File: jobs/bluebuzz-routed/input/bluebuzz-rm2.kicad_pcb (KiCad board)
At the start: 6 copper layers, 26 x 56.8 mm, 109 parts, among them J1 USB-C, J2 BAT, J3 SWD, J4 MOT, J5 TP, J6 PROBE, Q1 AO3400A, Q2 AO3400A, Q3 2N7002, SW1 PWR, U1 RP2350A, U10 USBLC6-2P6, U11 TPS22918DBVR, U2 BQ24074RGT, U20 DPS368, U21 DPS368, U22 DPS368, U23 DPS368, U3 TLV75533PDBV, U30 LSM6DS3TR-C, U40 MP34DT05-A, U5 TPS22918DBVR, U6 W25Q32JVUUIQ, U7 RM2, Y1 12MHz

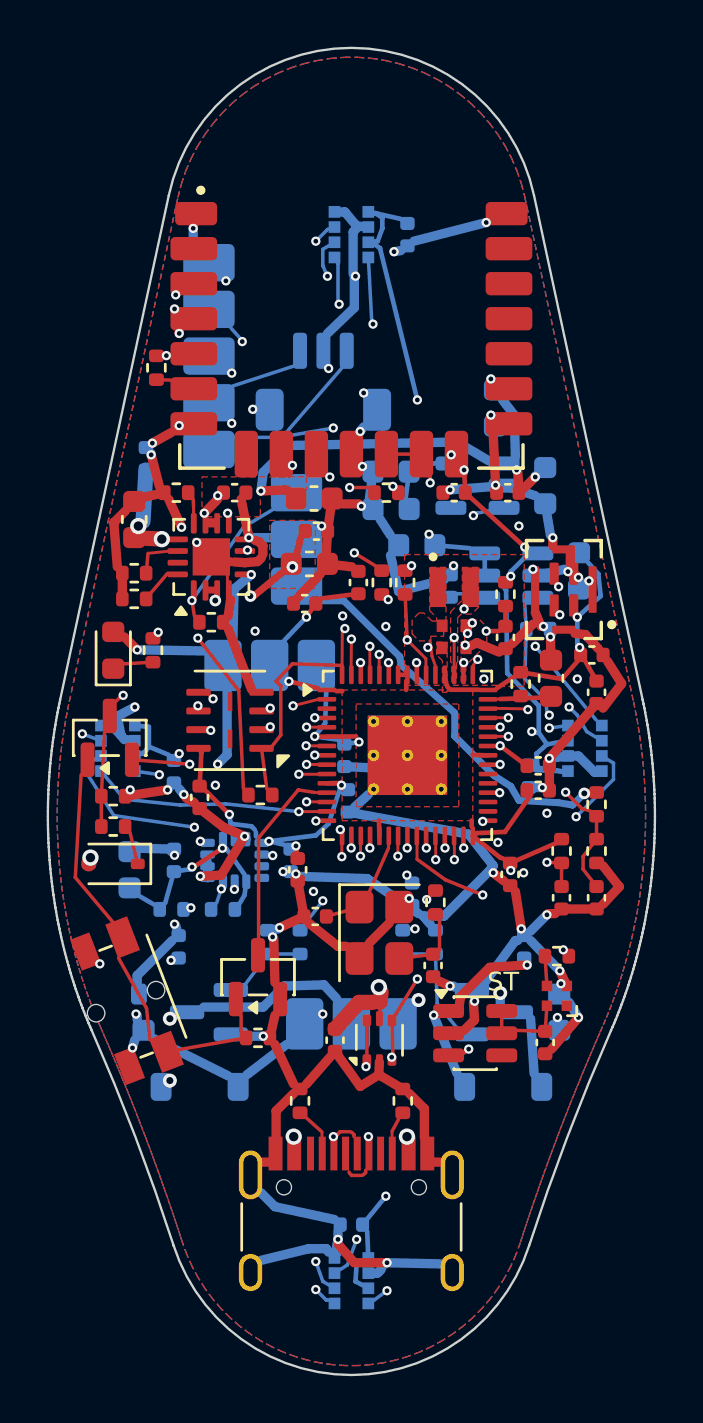
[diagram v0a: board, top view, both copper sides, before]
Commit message: Core: differential pairs routed coupled; both boards re-solved with their USB pairs
--diff-pairs finds pairs by net name (USB_DP/USB_DM, USB_C_DP/USB_C_DN, CLK_P/CLK_N, A+/A-),
takes a pad of each net close together as a pair's end, and routes each run between ends as one
centreline, wide enough for both tracks and the class's diff-pair gap, on a single layer; the
two tracks are laid along it and the router adds the pad legs. Runs go after the fine-pitch
escapes, so they block no pins, and are kept apart from copper the router may rip or pull.
The studio turns it on by default ("Route USB pairs side by side").

The cleanup cuts a track loose at both ends back to its outermost joints and cuts a tail back
to a joint already inside it, so no pair run is left dangling.

Re-solved (KiCad: 0 unconnected, 0 errors): earring-routed with USB_DP/DM 86%/78% coupled,
earring-locked-routed 92%/79%, bluebuzz-routed USB_DP/DM 81%/80% with 0.18 mm skew (the
hand-routed board: 31%). From bare pads, one thread: earring 5 of 6 seeds connected (was 4),
bluebuzz 6 of 6. examples/pair_check measures coupling.

Co-Authored-By: Claude Opus 5.5 (1M context) <noreply@anthropic.com>
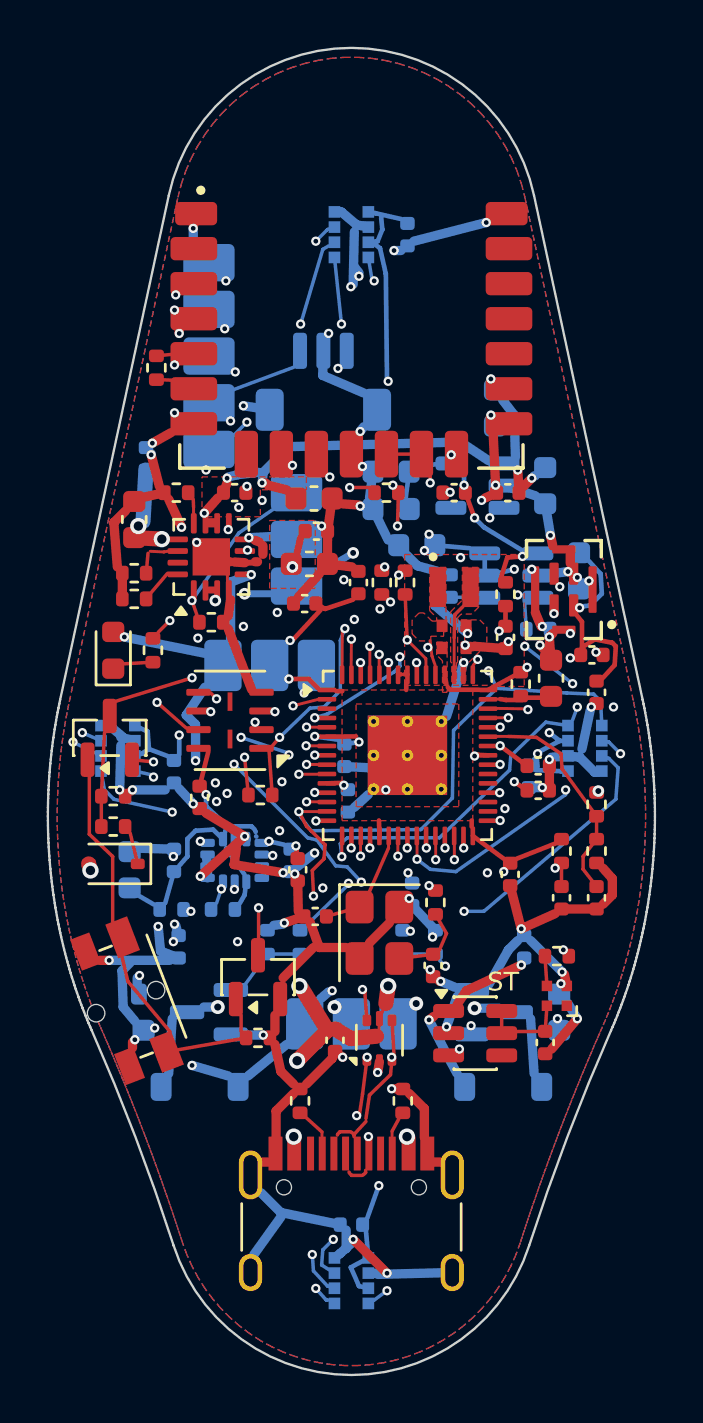
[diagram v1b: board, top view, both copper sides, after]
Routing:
- net QSPI_SD3: track 9.80 -> 25.7 mm, vias 2 -> 4
- net GND: track 191.6 -> 178.6 mm, vias 61 -> 71
- net TAC_SDO: track 66.7 -> 76.9 mm
- net USB_DM: track 36.1 -> 28.6 mm, vias 5 -> 2
- net SWCLK: track 30.8 -> 35.8 mm, vias 4 -> 6
- net PWR_HOLD: track 20.4 -> 16.6 mm, vias 2 -> 3
- net SWDIO: track 34.3 -> 30.7 mm, vias 3 -> 6
- net TAC_SDI: track 71.3 -> 74.3 mm
- net PG_N: track 12.5 -> 15.5 mm, vias 2 -> 3
- net IMU_INT1: track 6.57 -> 9.19 mm, vias 2 -> 4
- net VBUS: track 46.3 -> 48.9 mm, vias 6 -> 8
- net TAC_CS2: track 14.5 -> 16.7 mm
- net WL_CLK: track 21.3 -> 22.8 mm, vias 2 -> 3
- net SENS_EN: track 19.6 -> 18.1 mm, vias 3 -> 2
- net 3V3_SYS: track 61.1 -> 62.5 mm, vias 16 -> 17
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
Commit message: Core: differential pairs length-matched, and the short pair coupled; jobs re-solved
Length matching (grid::match_lengths): after the cleanup each pair's nets are measured end to
end along their copper and the shorter one is given bumps, one at a time, the tallest that lays,
on uncoupled tracks first; a bump that does not reduce the skew is undone.

The short pair: pins of a pair whose ends share a layer are left out of the fan-out, a run's
layer is chosen by cost (length, a price per via its ends need, how far from the pins it
starts) with each layer trying its nearest start ring first, and pair runs may cross pours,
kept block planes included, to be refilled round them. bluebuzz's resistor-to-RP2350 pair now
runs side by side on F.Cu with no via.

Re-solved (KiCad: 0 unconnected, 0 errors, no part moved): earring-routed, pairs 0.00 and 0.16
mm apart; earring-locked-routed 0.00 and 0.00; bluebuzz-routed 0.00 (76%/72% side by side)
and 0.13 mm (58%/60%). job.json `args` gives the studio the seed each job routes best with.

Co-Authored-By: Claude Opus 5.5 (1M context) <noreply@anthropic.com>
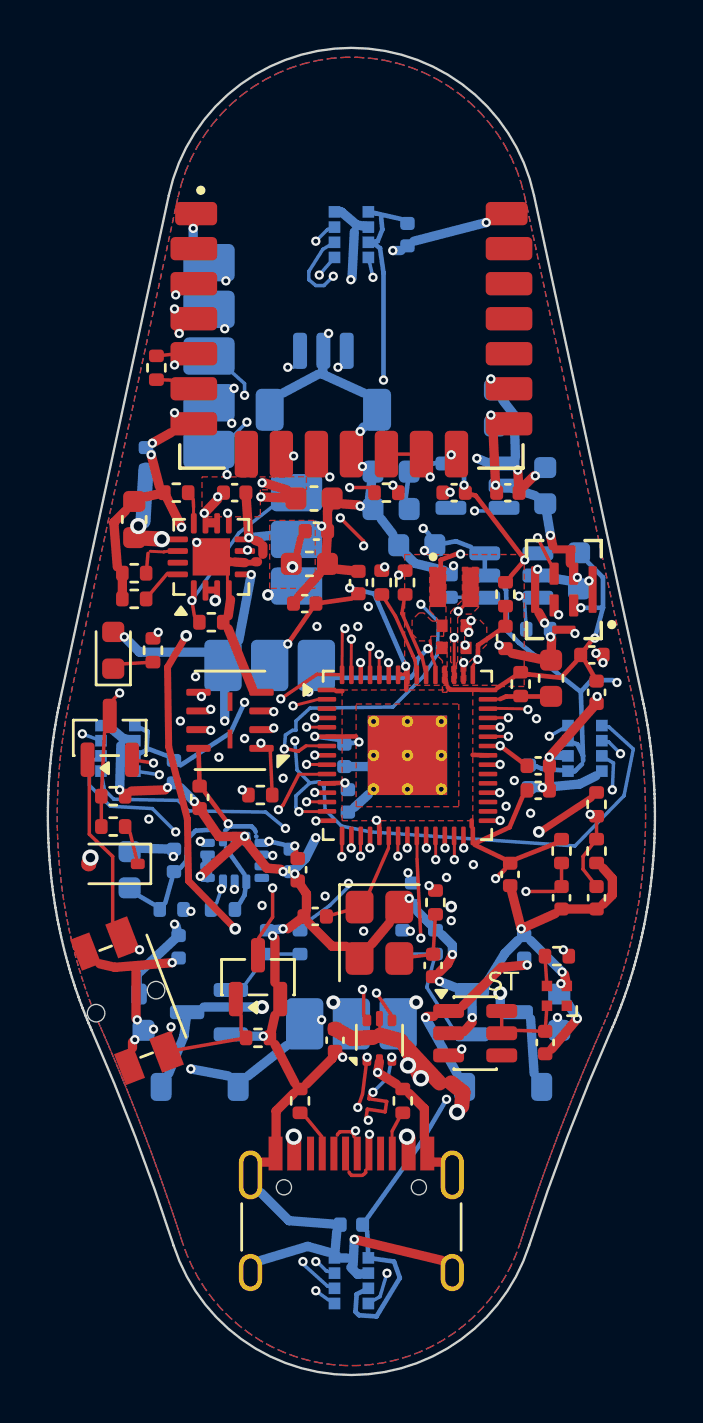
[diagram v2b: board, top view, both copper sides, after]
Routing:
- net VBAT: track 20.9 -> 37.7 mm, vias 5 -> 7
- net QSPI_SD3: track 25.7 -> 11.0 mm, vias 4 -> 3
- net TAC_SDO: track 76.9 -> 66.9 mm, vias 6 -> 7
- net VBUS: track 48.9 -> 58.3 mm
- net 3V3_SENS: track 75.4 -> 83.3 mm, vias 8 -> 6
- net PWR_HOLD: track 16.6 -> 23.2 mm, vias 3 -> 6
- net TAC_SCK: track 71.7 -> 77.8 mm
- net GND: track 178.6 -> 173.1 mm, vias 71 -> 63
- net 1V1: track 25.3 -> 29.8 mm, vias 7 -> 8
- net TAC_CS3: track 14.7 -> 18.0 mm, vias 4 -> 2
- net TAC_SDI: track 74.3 -> 76.9 mm, vias 5 -> 7
- net 3V3_SYS: track 62.5 -> 65.1 mm, vias 17 -> 15
- net IMU_INT1: track 9.19 -> 6.60 mm, vias 4 -> 2
- net SWCLK: track 35.8 -> 33.4 mm, vias 6 -> 5
- net PDM_CLK: track 8.12 -> 10.4 mm
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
